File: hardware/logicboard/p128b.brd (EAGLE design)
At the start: 80 x 80 mm, 43 parts, among them IC1 74LS595N, IC10 74LS595N, IC11 74LS595N, IC12 74LS595N, IC13 74LS595N, IC14 74LS595N, IC15 74LS595N, IC16 74LS595N, IC2 74LS595N, IC3 74LS595N, IC4 74LS595N, IC5 74LS595N, IC6 74LS595N, IC7 74LS595N, IC8 74LS595N, IC9 74LS595N

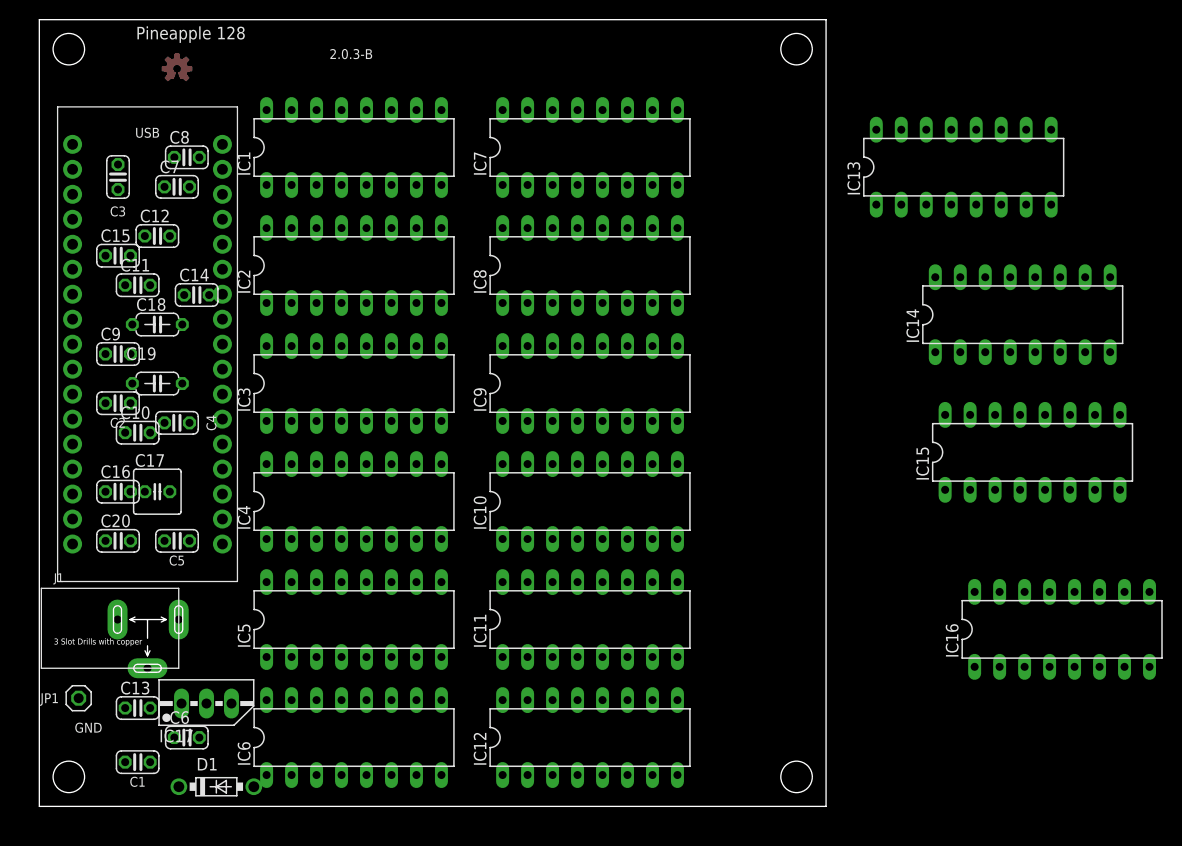
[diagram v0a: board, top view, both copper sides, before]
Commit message: Separated into 2 boards.
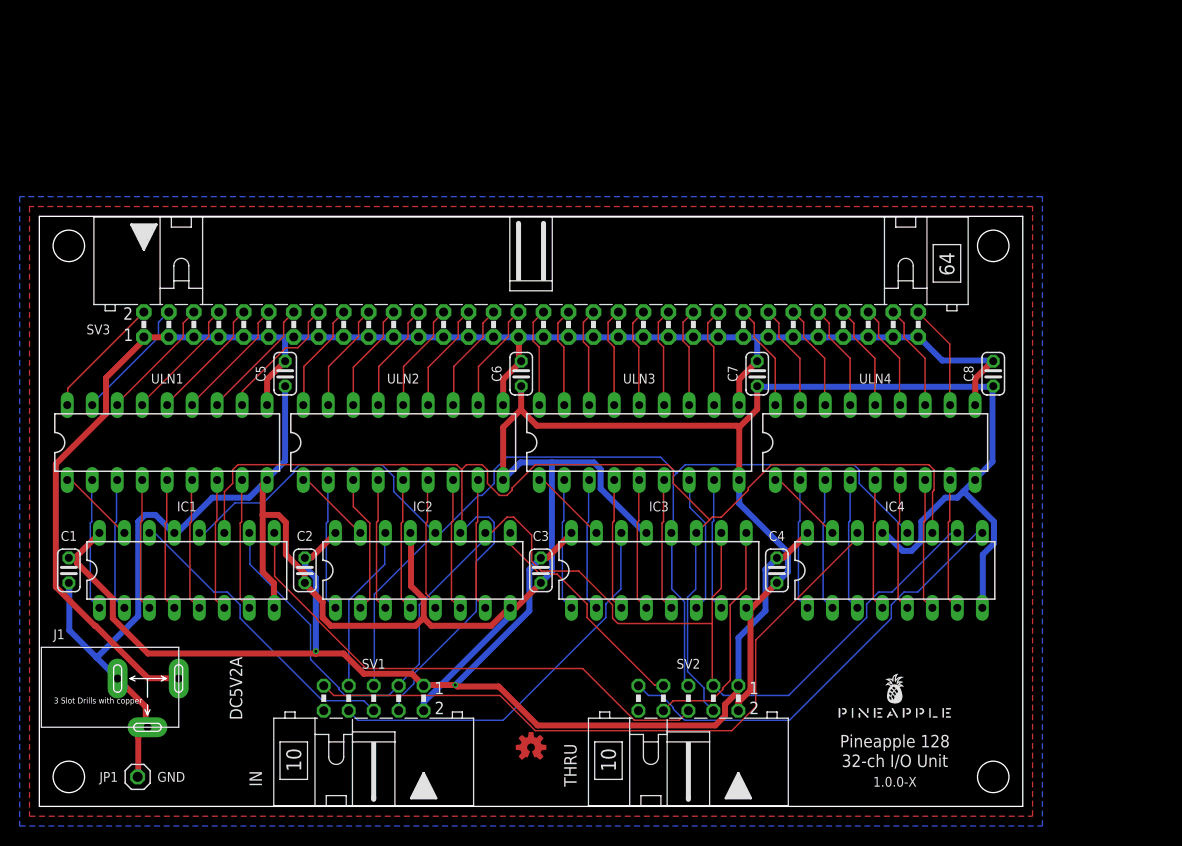
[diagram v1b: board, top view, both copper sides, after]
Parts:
- removed C10, C15: 10n, rcl:C025-024X044
- removed C11, C12, C13, C14, C16, C9: 10n, resistor:C025-024X044
- removed C17: (no value), rcl:C025-050X050
- removed C18, C19: (no value), rcl:C050-024X044
- removed C20: (no value), rcl:C025-024X044
- removed D1: 1N5817-B, diode:DO41-7.6
- removed IC10, IC11, IC12, IC13, IC14, IC15, IC16, IC5, IC6, IC7, IC8, IC9: 74LS595N, 74xx-us:DIL16
- removed IC17: (no value), v-reg:78MXXS
- removed MC1: ARDUINOMICRO, adafruit:ARDUINOMICRO
- added SV1, SV2: (no value), con-ml:ML10L
- added SV3: (no value), con-ml:ML64L
- added ULN1, ULN2, ULN3, ULN4: (no value), SparkFun-IC-Special-Function:DIL18
- moved C8 84.9 mm to (97.0, 44.0), turned to 270 degrees
- moved U$1 79.2 mm to (87.0, 9.00), flipped to the top
- moved LOGO1 77.8 mm to (50.0, 6.00)
- moved C4 62.8 mm to (75.0, 24.0), turned to 270 degrees
- moved C7 62.0 mm to (73.0, 44.0), turned to 270 degrees
- moved C3 58.7 mm to (51.0, 24.0)
- moved IC4 55.4 mm to (87.0, 24.0)
- moved C6 50.2 mm to (49.0, 44.0), turned to 270 degrees
- moved IC1 46.2 mm to (15.0, 24.0)
- moved IC3 36.4 mm to (63.0, 24.0)
- moved IC2 31.8 mm to (39.0, 24.0)
- moved C2 25.5 mm to (27.0, 24.0), turned to 270 degrees
- moved C1 20.7 mm to (3.00, 24.0), turned to 270 degrees
- moved C5 20.2 mm to (25.0, 44.0), turned to 270 degrees
- moved JP1 10.0 mm to (10.0, 3.00)
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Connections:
- removed net N$1: IC1.9, IC2.14
- removed net N$2: IC3.9, IC4.14
- removed net N$3: IC5.9, IC6.14
- removed net N$4: IC7.9, IC8.14
- removed net N$5: IC10.14, IC9.9
- removed net N$6: IC11.9, IC12.14
- removed net N$7: IC13.9, IC14.14
- removed net N$8: C17.1, C18.1, D1.C, IC17.IN, J1.+
- removed net N$9: IC15.9, IC16.14
- removed net Q100: IC13.3
- removed net Q101: IC13.4
- removed net Q102: IC13.5
- removed net Q103: IC13.6
- removed net Q104: IC13.7
- removed net Q105: IC14.15
- removed net Q106: IC14.1
- removed net Q107: IC14.2
- removed net Q108: IC14.3
- removed net Q109: IC14.4
- removed net Q110: IC14.5
- removed net Q111: IC14.6
- removed net Q112: IC14.7
- removed net Q113: IC15.15
- removed net Q114: IC15.1
- removed net Q115: IC15.2
- removed net Q116: IC15.3
- removed net Q117: IC15.4
- removed net Q118: IC15.5
- removed net Q119: IC15.6
- removed net Q120: IC15.7
- removed net Q121: IC16.15
- removed net Q122: IC16.1
- removed net Q123: IC16.2
- removed net Q124: IC16.3
- removed net Q125: IC16.4
- removed net Q126: IC16.5
- removed net Q127: IC16.6
- removed net Q128: IC16.7
- removed net Q33: IC5.15
- removed net Q34: IC5.1
- removed net Q35: IC5.2
- removed net Q36: IC5.3
- removed net Q37: IC5.4
- removed net Q38: IC5.5
- removed net Q39: IC5.6
- removed net Q40: IC5.7
- removed net Q41: IC6.15
- removed net Q42: IC6.1
- removed net Q43: IC6.2
- removed net Q44: IC6.3
- removed net Q45: IC6.4
- removed net Q46: IC6.5
- removed net Q47: IC6.6
- removed net Q48: IC6.7
- removed net Q49: IC7.15
- removed net Q50: IC7.1
- removed net Q51: IC7.2
- removed net Q52: IC7.3
- removed net Q53: IC7.4
- removed net Q54: IC7.5
- removed net Q55: IC7.6
- removed net Q56: IC7.7
- removed net Q57: IC8.15
- removed net Q58: IC8.1
- removed net Q59: IC8.2
- removed net Q60: IC8.3
- removed net Q61: IC8.4
- removed net Q62: IC8.5
- removed net Q63: IC8.6
- removed net Q64: IC8.7
- removed net Q65: IC9.15
- removed net Q66: IC9.1
- removed net Q67: IC9.2
- removed net Q68: IC9.3
- removed net Q69: IC9.4
- removed net Q70: IC9.5
- removed net Q71: IC9.6
- removed net Q72: IC9.7
- removed net Q73: IC10.15
- removed net Q74: IC10.1
- removed net Q75: IC10.2
- removed net Q76: IC10.3
- removed net Q77: IC10.4
- removed net Q78: IC10.5
- removed net Q79: IC10.6
- removed net Q80: IC10.7
- removed net Q81: IC11.15
- removed net Q82: IC11.1
- removed net Q83: IC11.2
- removed net Q84: IC11.3
- removed net Q85: IC11.4
- removed net Q86: IC11.5
- removed net Q87: IC11.6
- removed net Q88: IC11.7
- removed net Q89: IC12.15
- removed net Q90: IC12.1
- removed net Q91: IC12.2
- removed net Q92: IC12.3
- removed net Q93: IC12.4
- removed net Q94: IC12.5
- removed net Q95: IC12.6
- removed net Q96: IC12.7
- removed net Q97: IC13.15
- removed net Q98: IC13.1
- removed net Q99: IC13.2
- removed net SER5: IC9.14, MC1.P$4
- removed net SER6: IC11.14, MC1.P$3
- removed net SER7: IC13.14, MC1.P$2
- removed net SER8: IC15.14, MC1.P$1
- new net COMM: C5.1, C6.1, C7.1, C8.1, J1.+, SV3.1, SV3.11, SV3.13, SV3.15, SV3.17, SV3.19, SV3.21, SV3.23, SV3.25, SV3.27, SV3.29, SV3.3, SV3.31, SV3.33, SV3.35, SV3.37, SV3.39, SV3.41, SV3.43, SV3.45, SV3.47, SV3.49, SV3.5, SV3.51, SV3.53, SV3.55, SV3.57, SV3.59, SV3.61, SV3.63, SV3.7, SV3.9, ULN1.10, ULN2.10, ULN3.10, ULN4.10
- new net OUT1: IC1.9, SV2.6
- new net OUT2: IC2.9, SV2.7
- new net OUT3: IC3.9, SV2.8
- new net OUT4: IC4.9, SV2.9
- new net X1: SV3.2, ULN1.18
- new net X10: SV3.20, ULN2.17
- new net X11: SV3.22, ULN2.16
- new net X12: SV3.24, ULN2.15
- new net X13: SV3.26, ULN2.14
- new net X14: SV3.28, ULN2.13
- new net X15: SV3.30, ULN2.12
- new net X16: SV3.32, ULN2.11
- new net X17: SV3.34, ULN3.18
- new net X18: SV3.36, ULN3.17
- new net X19: SV3.38, ULN3.16
- new net X2: SV3.4, ULN1.17
- new net X20: SV3.40, ULN3.15
- new net X21: SV3.42, ULN3.14
- new net X22: SV3.44, ULN3.13
- new net X23: SV3.46, ULN3.12
- new net X24: SV3.48, ULN3.11
- new net X25: SV3.50, ULN4.18
- new net X26: SV3.52, ULN4.17
- new net X27: SV3.54, ULN4.16
- new net X28: SV3.56, ULN4.15
- new net X29: SV3.58, ULN4.14
- new net X3: SV3.6, ULN1.16
- new net X30: SV3.60, ULN4.13
- new net X31: SV3.62, ULN4.12
- new net X32: SV3.64, ULN4.11
- new net X4: SV3.8, ULN1.15
- new net X5: SV3.10, ULN1.14
- new net X6: SV3.12, ULN1.13
- new net X7: SV3.14, ULN1.12
- new net X8: SV3.16, ULN1.11
- new net X9: SV3.18, ULN2.18
- net GND: now also SV1.2, SV2.2, ULN1.9, ULN2.9, ULN3.9, ULN4.9; no longer C10.2, C11.2, C12.2, C13.2, C14.2, C15.2, C16.2, C17.2, C18.2, C19.2, C20.2, C9.2, IC10.13, IC10.8, IC11.13, IC11.8, IC12.13, IC12.8, IC13.13, IC13.8, IC14.13, IC14.8, IC15.13, IC15.8, IC16.13, IC16.8, IC17.GND, IC5.13, IC5.8, IC6.13, IC6.8, IC7.13, IC7.8, IC8.13, IC8.8, IC9.13, IC9.8, MC1.P$12, MC1.P$21
- net Q1: now also ULN1.1
- net Q10: now also ULN2.2
- net Q11: now also ULN2.3
- net Q12: now also ULN2.4
- net Q13: now also ULN2.5
- net Q14: now also ULN2.6
- net Q15: now also ULN2.7
- net Q16: now also ULN2.8
- net Q17: now also ULN3.1
- net Q18: now also ULN3.2
- net Q19: now also ULN3.3
- net Q2: now also ULN1.2
- net Q20: now also ULN3.4
- net Q21: now also ULN3.5
- net Q22: now also ULN3.6
- net Q23: now also ULN3.7
- net Q24: now also ULN3.8
- net Q25: now also ULN4.1
- net Q26: now also ULN4.2
- net Q27: now also ULN4.3
- net Q28: now also ULN4.4
- net Q29: now also ULN4.5
- net Q3: now also ULN1.3
- net Q30: now also ULN4.6
- net Q31: now also ULN4.7
- net Q32: now also ULN4.8
- net Q4: now also ULN1.4
- net Q5: now also ULN1.5
- net Q6: now also ULN1.6
- net Q7: now also ULN1.7
- net Q8: now also ULN1.8
- net Q9: now also ULN2.1
- net RCLK: now also SV1.5, SV2.5; no longer IC10.12, IC11.12, IC12.12, IC13.12, IC14.12, IC15.12, IC16.12, IC5.12, IC6.12, IC7.12, IC8.12, IC9.12, MC1.P$9
- net SER1: now also SV1.6; no longer MC1.P$8
- net SER2: now also IC2.14, SV1.7; no longer IC3.14, MC1.P$7
- net SER3: now also IC3.14, SV1.8; no longer IC5.14, MC1.P$6
- net SER4: now also IC4.14, SV1.9; no longer IC7.14, MC1.P$5
- net SRCLK: now also SV1.4, SV2.4; no longer IC10.11, IC11.11, IC12.11, IC13.11, IC14.11, IC15.11, IC16.11, IC5.11, IC6.11, IC7.11, IC8.11, IC9.11, MC1.P$10
- net SRCLR: now also SV1.3, SV2.3; no longer IC10.10, IC11.10, IC12.10, IC13.10, IC14.10, IC15.10, IC16.10, IC5.10, IC6.10, IC7.10, IC8.10, IC9.10, MC1.P$11
- net VCC: now also SV1.1, SV2.1; no longer C10.1, C11.1, C12.1, C13.1, C14.1, C15.1, C16.1, C19.1, C20.1, C5.1, C6.1, C7.1, C8.1, C9.1, D1.A, IC10.16, IC11.16, IC12.16, IC13.16, IC14.16, IC15.16, IC16.16, IC17.OUT, IC5.16, IC6.16, IC7.16, IC8.16, IC9.16, MC1.P$23
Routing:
- net GND: track 0.00 -> 307.9 mm
- net COMM: track 0.00 -> 161.6 mm
- net SRCLK: track 0.00 -> 150.0 mm
- net VCC: track 0.00 -> 136.7 mm, vias 0 -> 2
- net RCLK: track 0.00 -> 128.2 mm
- net SRCLR: track 0.00 -> 125.1 mm
- net SER4: track 0.00 -> 68.8 mm
- net OUT1: track 0.00 -> 53.0 mm
- net OUT4: track 0.00 -> 45.2 mm
- net SER3: track 0.00 -> 40.2 mm
- net SER1: track 0.00 -> 31.1 mm
- net OUT3: track 0.00 -> 23.8 mm
- net OUT2: track 0.00 -> 23.5 mm
- net SER2: track 0.00 -> 17.1 mm
- net Q11: track 0.00 -> 14.1 mm
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- added copper zone on layer 1, net GND
- added copper zone on layer 16, net GND
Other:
- board size 80 x 80 mm -> 100 x 60 mm
- board text added: "1.0.0-X"
- board text added: "32-ch I/O Unit"
- board text added: "DC5V2A"
- board text added: "IN"
- board text added: "THRU"
- board text removed: "2.0.3-B"
- board text removed: "USB"
